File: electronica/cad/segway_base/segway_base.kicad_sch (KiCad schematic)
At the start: 145 parts, among them J1 XT60PW-M 1=P− 2=P+, J10 XH-6 mot+enc DER, J11 Motor IZQ a módulo, J12 Motor DER a módulo, J13 Servo IZQ JR, J14 Servo DER JR, J15 UBEC entrada, J16 UBEC salida bornera, J17 UBEC salida enchufe, J18 Voltímetro ROB-004, J19 LM2596 entrada, J2 MKDS3 batería alt., J20 LM2596 salida 5V, J21 Shunt INA219 IZQ 1=Vin− 2=Vin+, J22 Shunt INA219 DER 1=Vin− 2=Vin+, J3 Lazo interruptor+paro, J4 Paro XH-3, J5 POWER DRV IZQ, J6 POWER DRV DER, J7 Encoder IZQ XH-4, J8 Encoder DER XH-4, J9 XH-6 mot+enc IZQ, Q1 IRF4905

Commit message: electronica: esquema v0.3 con Blue Pill STM32F103C8T6 (ELE-020)
- Especificación v0.3: 153 componentes, 63 nets, 7 símbolos de módulos;
  módulos enchufados en zócalos de 2,54 mm y motores en borneras (DEC-13).
- Encoders en TIM2/TIM4, PWM de motores en TIM3, servos en TIM1, I2C2,
  rail 3V3 de periféricos con mini buck ROB-005.
- Datasheet STM32F103 DS5319 y material de la Blue Pill archivados.
- ERC 0 errores/0 avisos y netlist igual a la especificación.

Co-Authored-By: Claude Opus 5.5 <noreply@anthropic.com>
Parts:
- removed A1: ESP32-DevKitC-32E (prov.), symbol segway_modulos:ROB-012_ESP32-DevKitC-V4_38p
- removed A3: DRV8871 mód. IZQ, Connector_PinSocket_2.54mm:PinSocket_1x04_P2.54mm_Vertical, symbol segway_modulos:ROB-008_DRV8871_modulo_4p
- removed A4: DRV8871 mód. DER (prov.), Connector_PinSocket_2.54mm:PinSocket_1x04_P2.54mm_Vertical, symbol segway_modulos:ROB-008_DRV8871_modulo_4p
- removed A5: INA219 MCU-219 0x41 IZQ, Connector_PinSocket_2.54mm:PinSocket_1x06_P2.54mm_Vertical, symbol segway_modulos:ROB-002_INA219_MCU-219_6p
- removed A6: INA219 MCU-219 0x44 DER, Connector_PinSocket_2.54mm:PinSocket_1x06_P2.54mm_Vertical, symbol segway_modulos:ROB-002_INA219_MCU-219_6p
- removed J1: XT60PW-M 1=P− 2=P+, Connector_AMASS:AMASS_XT60PW-M_1x02_P7.20mm_Horizontal, symbol Connector_Generic:Conn_01x02
- removed J10: XH-6 mot+enc DER, Connector_JST:JST_XH_B6B-XH-A_1x06_P2.50mm_Vertical, symbol Connector_Generic:Conn_01x06
- removed J17: UBEC salida enchufe, Connector_PinHeader_2.54mm:PinHeader_1x03_P2.54mm_Vertical, symbol Connector_Generic:Conn_01x03
- removed J19: LM2596 entrada, TerminalBlock_Phoenix:TerminalBlock_Phoenix_MKDS-1,5-2-5.08_1x02_P5.08mm_Horizontal, symbol Connector:Screw_Terminal_01x02
- removed J2: MKDS3 batería alt., TerminalBlock_Phoenix:TerminalBlock_Phoenix_MKDS-3-2-5.08_1x02_P5.08mm_Horizontal, symbol Connector:Screw_Terminal_01x02
- removed J20: LM2596 salida 5V, TerminalBlock_Phoenix:TerminalBlock_Phoenix_MKDS-1,5-2-5.08_1x02_P5.08mm_Horizontal, symbol Connector:Screw_Terminal_01x02
- removed J4: Paro XH-3, Connector_JST:JST_XH_B3B-XH-A_1x03_P2.50mm_Vertical, symbol Connector_Generic:Conn_01x03
- removed J7: Encoder IZQ XH-4, Connector_JST:JST_XH_B4B-XH-A_1x04_P2.50mm_Vertical, symbol Connector_Generic:Conn_01x04
- removed J8: Encoder DER XH-4, Connector_JST:JST_XH_B4B-XH-A_1x04_P2.50mm_Vertical, symbol Connector_Generic:Conn_01x04
- removed J9: XH-6 mot+enc IZQ, Connector_JST:JST_XH_B6B-XH-A_1x06_P2.50mm_Vertical, symbol Connector_Generic:Conn_01x06
- removed JP2: AD0 1-2=GND, Jumper:SolderJumper-3_P1.3mm_Bridged12_RoundedPad1.0x1.5mm, symbol Jumper:SolderJumper_3_Bridged12
- added A1: Blue Pill STM32F103C8T6, symbol segway_modulos:ROB-012_BluePill_STM32F103C8_40p
- added A10: LM2596 ROB-001 5V (respaldo), symbol segway_modulos:ROB-001_LM2596_modulo_4p
- added A3: DRV8871 mód. IZQ (enchufable), symbol segway_modulos:ROB-008_DRV8871_modulo_8p
- added A4: DRV8871 mód. DER (prov., enchufable), symbol segway_modulos:ROB-008_DRV8871_modulo_8p
- added A5: INA219 MCU-219 0x41 IZQ, symbol segway_modulos:ROB-002_INA219_MCU-219_8p
- added A6: INA219 MCU-219 0x44 DER, symbol segway_modulos:ROB-002_INA219_MCU-219_8p
- added A9: Mini buck 3,3V ROB-005 (3V3_PER), symbol segway_modulos:ROB-005-006_MiniBuck_modulo_4p
- added C27: 10µ/10V X7R, Capacitor_SMD:C_1206_3216Metric_Pad1.33x1.80mm_HandSolder, symbol Device:C
- added C28: 100n/50V X7R, Capacitor_SMD:C_0805_2012Metric_Pad1.18x1.45mm_HandSolder, symbol Device:C
- added J1: Batería MKDS3 1=P− 2=P+, TerminalBlock_Phoenix:TerminalBlock_Phoenix_MKDS-3-2-5.08_1x02_P5.08mm_Horizontal, symbol Connector:Screw_Terminal_01x02
- added J23: UART1 1=GND 2=TX 3=RX, Connector_PinHeader_2.54mm:PinHeader_1x03_P2.54mm_Vertical, symbol Connector_Generic:Conn_01x03
- added J4: Paro MPT0,5 1=GND 2=NC 3=AUX, TerminalBlock_Phoenix:TerminalBlock_Phoenix_MPT-0,5-3-2.54_1x03_P2.54mm_Horizontal, symbol Connector:Screw_Terminal_01x03
- added J7: Encoder IZQ PT1,5 1=GND 2=A 3=B 4=V, TerminalBlock_Phoenix:TerminalBlock_Phoenix_PT-1,5-4-3.5-H_1x04_P3.50mm_Horizontal, symbol Connector:Screw_Terminal_01x04
- added J8: Encoder DER PT1,5 1=GND 2=A 3=B 4=V, TerminalBlock_Phoenix:TerminalBlock_Phoenix_PT-1,5-4-3.5-H_1x04_P3.50mm_Horizontal, symbol Connector:Screw_Terminal_01x04
- added R32: 0 (3V3_MCU↔3V3_PER), Resistor_SMD:R_0805_2012Metric_Pad1.20x1.40mm_HandSolder, symbol Device:R
- added R33, R34: 1k, Resistor_SMD:R_0805_2012Metric_Pad1.20x1.40mm_HandSolder, symbol Device:R
- added R35, R36, R37, R38: 4k7 1%, Resistor_SMD:R_0805_2012Metric_Pad1.20x1.40mm_HandSolder, symbol Device:R
- added R39: 0 (AD0→GND), Resistor_SMD:R_0805_2012Metric_Pad1.20x1.40mm_HandSolder, symbol Device:R
- added R40: 1k (AD0→3V3_PER), Resistor_SMD:R_0805_2012Metric_Pad1.20x1.40mm_HandSolder, symbol Device:R
- added TP41: TP_3V3_MCU, TestPoint:TestPoint_Loop_D2.50mm_Drill1.0mm, symbol Connector:TestPoint
- A2: Estado provisorio [H] (orden de pines [V]/[M]; zócalo estándar 1x08; contorno del módulo pendiente de medida) -> provisorio [H] (orden de pines [V]/[M]; zócalo estándar 1x08 (DEC-13); alimentado desde 3V3_PER; contorno del módulo pendiente de medida; codificación propuesta: retirar el pin 5 (XDA, sin uso) de la tira macho y tapar la posición 5 del zócalo, porque invertido llevaría 3V3_PER a INT y el VCC del módulo a PB14)
- A7: Estado provisorio [H] (orden [V]; dirección de fábrica 0x40 [H], sujeta a aprobar el cambio del contrato §4.1; ubicación en la rama lógica = propuesta [H] que se desvía de [ENERGIA] §5.2 (INA226 en el bus), pendiente de Matías, REQ-14; unión VBS-IN− interna pendiente E-01) -> provisorio [H] (orden [V]; dirección de fábrica 0x40 [H], sujeta a aprobar el cambio del contrato §4.1; ubicación en la rama lógica = propuesta [H] que se desvía de [ENERGIA] §5.2 (INA226 en el bus), pendiente de Matías, REQ-14; unión VBS-IN− interna pendiente E-01; la 1x08 no tiene pin libre para codificar: invertido lleva VM_LOG_F a VCC (6 V abs.) y deja el shunt entre 3V3_PER y GND, así que la huella lleva un tope mecánico contra el cuerpo invertido y el contorno serigrafiado); Fuente [CAP]/ROB-009_INA226/referencia_compra.png [V]; [DS-226] p.3, p.5, p.15, p.18 Tabla 6-2, p.26-28; [ENERGIA] §5.1 (R100 solo apto para lógica) -> [CAP]/ROB-009_INA226/referencia_compra.png [V]; [DS-226] p.3, p.5, p.15, p.18 Tabla 6-2, p.26-28; [ENERGIA] §5.1 (R100 solo apto para lógica); [DS-226] p.4 §5.1 (VS 6 V abs.)
- A8: Estado pendiente de medida (propuesta de [ENERGIA] §10.1, pendiente de Matías; chip no identificado; huella sin medir; validar en E-02) -> pendiente de medida (propuesta de [ENERGIA] §10.1, pendiente de Matías; chip no identificado; huella de 4 PinSocket_1x01 en las esquinas medidas, a crear tras E-01 (DEC-13); validar en E-02; cuatro esquinas: girado 180° une VM_LOG con 5V por la masa del módulo e invierte su entrada, así que la huella necesita codificación mecánica (propuesta 16); zócalos superpuestos con los de A10 para que no entren los dos)
- C10, C11, C12, C13: Estado provisorio [H] (DNP; el pad recibe 2 kΩ como resistencia in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 -> provisorio [H] (DNP; 2 kΩ en el pad solo si E-04 confirma s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; Fuente [DS-ESP32] p.38-39 (filtro del PCNT) -> [RM0008] §13.3 (filtro digital ICxF del timer); divisor 1k/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
- C14: Fuente [DS-ESP32] p.43 Tabla 4-3 (100 nF de ensayo) -> [DS-STM32] p.75 Ecuación 1 (carga del capacitor de muestreo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
- C15: Fuente Filtro RC [H]: activación (contacto abierto) τ = (R24 + R25)·C15 ≈ 1,1 ms, ≈1,5 ms hasta VIH = 0,75·VDD; liberación τ = R25·C15 = 0,1 ms -> Filtro RC [H]: activación (contacto abierto) τ = (R24 + R25)·C15 ≈ 1,1 ms, ≈1,15 ms hasta VIH = 2,145 V; liberación τ = R25·C15 = 0,1 ms
- C25: Fuente [DS-ESP32] p.19, p.52 -> [STM32-BASE] (pin 5V = VBUS sin protección); [SCH-BP] (C5 1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
- C26: Estado provisorio [H] (DNP) -> provisorio [H] (DNP; ahora en 3V3_MCU); Fuente LDO AMS1117 de la placa: estabilidad con cerámicos no docum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 -> [SCH-BP] (C6 10 µF + C8 100 nF ya en la salida del LDO de l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
- D2: Estado provisorio [H] (no reemplazar por 0 Ω salvo verificar que e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 -> provisorio [H] (obligatoria, nunca 0 Ω: impide que el USB a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; Fuente [SCH-DevKitC] (D3 BAT760-7 VBUS→EXT_5V); [CONTRATO] §2.11(b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 -> [SCH-BP] (VBUS del micro-USB unido directo al pin 5V); [STM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
- D3: DNP si -> (none); Estado provisorio [H] (DNP con Q1) -> provisorio [H] (montado con Q1; limita VGS a 12 V); now fitted
- F2: value ATM lento PEND (antec. 5A) -> ATM lento PEND (≤4 A); Estado provisorio [H] (valor tras E-04 y ≤ corriente admisible de 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 -> provisorio [H] (≤ 4 A por los zócalos de A3 y A5: 2 contact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
- F3: value ATM lento PEND (antec. 5A) -> ATM lento PEND (≤4 A); Estado provisorio [H] (valor tras E-04 y ≤ corriente admisible de 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 -> provisorio [H] (≤ 4 A por los zócalos de A4 y A6; valor tra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
- F5: value ATM lento PEND -> ATM rápido PEND (prop. ≤1A); Estado provisorio [H] (valor tras E-02; decisión 8 de [ENERGIA] §1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 -> provisorio [H] (propuesta 17: ≤ 1 A de acción rápida, que a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; Fuente [ENERGIA] §2.2 (fila Lógica) -> [ENERGIA] §2.2 (fila Lógica); consumo de la rama ≈0,1 A [H]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
- J11: value Motor IZQ a módulo -> Motor IZQ 1=M− 2=M+; DNP si -> (none); Estado provisorio [H] (DNP; solo con J9/J10, cuyo orden es [H]) -> provisorio [H] (montada; 1 = M− blanco = OUT2, 2 = M+ rojo 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; Fuente [DS-DRV] p.3 (OUT1/OUT2); [INV] ROB-011 (rojo M+, blanco M−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 -> DEC-13 [M] (borneras para motores); DEC-01 [M] (rojo M+, bl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; now fitted
- J12: value Motor DER a módulo -> Motor DER 1=M− 2=M+; DNP si -> (none); Estado provisorio [H] (DNP; solo con J9/J10, cuyo orden es [H]) -> provisorio [H] (montada; 1 = M− blanco = OUT2, 2 = M+ rojo 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; Fuente [DS-DRV] p.3 (OUT1/OUT2); [INV] ROB-011 (rojo M+, blanco M−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 -> Igual que J11; now fitted
- J13, J14: Estado provisorio [H] (orden JR GND-V+-SIG [D distribuidor], verificar en el ejemplar E-01/E-05; contacto de 2,54 mm ≈3 A [H] < bloqueo 3,1-3,9 A: medir la temperatura del contacto con el servo bloqueado en E-05/E-06) -> provisorio [H] (orden JR GND-V+-SIG [D distribuidor], verificar en el ejemplar E-01/E-05; contacto de 2,54 mm ≈3 A [H] < bloqueo 3,1-3,9 A: medir la temperatura del contacto con el servo bloqueado en E-05/E-06; serigrafiar 'S + −' y los colores del cable junto al header)
- J15: Estado provisorio [H] (tipo de enchufe pendiente) -> provisorio [H] (montada; se corta el enchufe rojo de 2 pine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; Fuente [CAP]/ROB-007_YSIDO_UBEC_6A/referencia_compra.png [V] -> [CAP]/ROB-007_YSIDO_UBEC_6A/referencia_compra.png [V]; DEC-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
- J16: value UBEC salida bornera -> UBEC salida 6V PT1,5 1=GND 2=V+; footprint TerminalBlock_Phoenix:TerminalBlock_Phoenix_MKDS-1,5-2-5.08_1x02_P5.08mm_Horizontal -> TerminalBlock_Phoenix:TerminalBlock_Phoenix_PT-1,5-2-3.5-H_1x02_P3.50mm_Horizontal; DNP si -> (none); Estado provisorio [H] (DNP; necesaria para operar con dos servos p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 -> provisorio [H] (montada; se corta el JR de salida del UBEC;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; Fuente [DS-SERVO] p.3 tabla 3-4 (bloqueo 3,1-3,9 A) -> DEC-13 [M]; [DS-SERVO] p.3 tabla 3-4 (bloqueo 3,9 A por ser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; now fitted
- J21: DNP (none) -> si; Estado provisorio [H] (cable a la bornera del módulo A5; corriente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 -> provisorio [H] (DNP; respaldo si el módulo A5 conserva su b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; now not fitted
- J22: DNP (none) -> si; Estado provisorio [H] (cable a la bornera del módulo A6; corriente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 -> provisorio [H] (DNP; respaldo si el módulo A6 conserva su b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; now not fitted
- J3: Estado provisorio [H] (REQ-17 abierto) -> provisorio [H] (REQ-17 abierto; igual tipo que J1: separarl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
- J5: value POWER DRV IZQ -> POWER DRV IZQ (opción A); DNP (none) -> si; Estado provisorio [H] -> provisorio [H] (DNP; solo en la opción A: módulo con sus bo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; now not fitted
- J6: value POWER DRV DER -> POWER DRV DER (opción A); DNP (none) -> si; Estado provisorio [H] -> provisorio [H] (DNP; solo en la opción A); now not fitted
- JP1: DNP (none) -> si; Estado provisorio [H] (excluyente con Q1; con JP1 la única protecc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 -> provisorio [H] (DNP; solo si Matías elige un XT60 en latigu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; now not fitted
- JP3: value SDA INA 1-2=I2C0 -> SDA INA 1-2=I2C2; Estado provisorio [H] (decisión tras E-08) -> provisorio [H] (1-2 = INA en I2C2, opción A; 2-3 = I2C1 rem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
- JP4: value SCL INA 1-2=I2C0 -> SCL INA 1-2=I2C2; Estado provisorio [H] (decisión tras E-08) -> provisorio [H] (1-2 = INA en I2C2, opción A; 2-3 = I2C1 rem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
- Q1: DNP si -> (none); Estado provisorio [H] (DNP; decisiones 3 y 9 de [ENERGIA] §10; a 1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 -> provisorio [H] (montado por defecto: con J1 en bornera es l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; now fitted
- R1: Estado provisorio [H] (decisión 14 de [ENERGIA] §10 pendiente de M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 -> provisorio [H] (lado MCU de R35; 2,2 kΩ cubre un pull-up in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; Fuente [ENERGIA] §8.1; [CONTRATO] §5.3; [DS-ESP32] p.52; [DS-DRV] 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 -> [DS-STM32] p.61 Tabla 36 (RPU 30-50 kΩ, fuga ±1 µA); [RM000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
- R10, R11, R12, R9: Fuente [CONTRATO] §2.4; [ENERGIA] §6.5; [DS-ESP32] p.52-53 -> [CONTRATO] §2.4; [ENERGIA] §6.5; [DS-STM32] Tabla 7 p.37 (i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
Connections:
- net 5V: now also A10.3 (OUT+)
- net CICLO_SCL1: now also A1.16 (PB8)
- net ENC_DER_A: now also J8.2 (Pin_2)
- net ENC_DER_A_MCU: now also A1.14 (PB6)
- net ENC_DER_B: now also J8.3 (Pin_3)
- net ENC_DER_B_MCU: now also A1.15 (PB7)
- net ENC_IZQ_A: now also J7.2 (Pin_2)
- net ENC_IZQ_A_MCU: now also A1.25 (PA0)
- net ENC_IZQ_B: now also J7.3 (Pin_3)
- net ENC_IZQ_B_MCU: now also A1.26 (PA1)
- net GND: now also A1.19 (GND), A1.39 (GND), A10.2 (IN-), A10.4 (OUT-), A3.1 (GND), A3.6 (POWER-), A4.1 (GND), A4.6 (POWER-), A5.2 (Gnd), A6.2 (Gnd), A9.2 (IN-), A9.4 (OUT-)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
- net I2C_SCL: now also A1.35 (PB10)
- net I2C_SDA: now also A1.36 (PB11)
- net IMU_AD0: now also R39.2, R40.2
- net IMU_INT: now also A1.3 (PB14)
- net IN1_DER: now also A4.3 (IN1), R37.2; no longer R3.1
- net IN1_IZQ: now also A3.3 (IN1), R35.2; no longer R1.1
- net IN2_DER: now also A4.4 (IN2), R38.2; no longer R4.1
- net IN2_IZQ: now also A3.4 (IN2), R36.2; no longer R2.1
- net INA_ALERT: now also A1.2 (PB13)
- net INA_SCL: now also A5.3 (Scl), A6.3 (Scl)
- net INA_SDA: now also A5.4 (Sda), A6.4 (Sda)
- net LED_ESTADO: now also A1.13 (PB5)
- net MOT_DER_1: now also J12.2 (Pin_2), A4.7 (OUT1); no longer J12.1 (Pin_1)
- net MOT_DER_2: now also J12.1 (Pin_1), A4.8 (OUT2); no longer J12.2 (Pin_2)
- net MOT_IZQ_1: now also J11.2 (Pin_2), A3.7 (OUT1); no longer J11.1 (Pin_1)
- net MOT_IZQ_2: now also J11.1 (Pin_1), A3.8 (OUT2); no longer J11.2 (Pin_2)
- net PARO_AUX: now also J4.3 (Pin_3)
- net PARO_CONT: now also J4.2 (Pin_2)
- net PARO_MCU: now also A1.1 (PB12)
- net RESERVA_SDA1: now also A1.17 (PB9)
- net SERVO_DER_MCU: now also A1.4 (PB15)
- net SERVO_IZQ_MCU: now also A1.5 (PA8)
- net VBAT_ADC: now also A1.28 (PA3)
- net VBAT_P: now also J1.2 (Pin_2)
- net VM_DER: now also A4.2 (VM), A4.5 (POWER+), A6.5 (Vin-), A6.7 (Vin-_born)
- net VM_DER_F: now also A6.6 (Vin+), A6.8 (Vin+_born)
- net VM_IZQ: now also A3.2 (VM), A3.5 (POWER+), A5.5 (Vin-), A5.7 (Vin-_born)
- net VM_IZQ_F: now also A5.6 (Vin+), A5.8 (Vin+_born)
- net VM_LOG: now also A10.1 (IN+), A9.1 (IN+), C28.1
- net V_ENC: now also J7.4 (Pin_4), J8.4 (Pin_4)
- net 3V3 renamed 3V3_PER
- net 3V3_PER: now also A5.1 (Vcc), A6.1 (Vcc), A9.3 (OUT+), C27.1, R32.2, R40.1; no longer C26.1, R24.1
- net 5V_ESP renamed 5V_MCU
- net 5V_MCU: now also A1.18 (5V)
- new net 3V3_MCU: A1.20 (3V3), A1.21 (VBAT), A1.38 (3V3), C26.1, R24.1, R32.1, TP41.1
- new net IN1_DER_MCU: A1.33 (PB0), R3.1, R37.1
- new net IN1_IZQ_MCU: A1.31 (PA6), R1.1, R35.1
- new net IN2_DER_MCU: A1.34 (PB1), R38.1, R4.1
- new net IN2_IZQ_MCU: A1.32 (PA7), R2.1, R36.1
- new net UART1_RX: J23.3 (Pin_3), R34.1
- new net UART1_RX_MCU: A1.7 (PA10), R34.2
- new net UART1_TX: J23.2 (Pin_2), R33.2
- new net UART1_TX_MCU: A1.6 (PA9), R33.1
- no-connect marks 23 -> 15
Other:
- note added: "BLUE PILL STM32"
- note removed: "CONTROLADOR ESP32 (PROVISORIO)"

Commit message: electronica: esquema v0.4 simplificado y PCB v0.1 en curso (pausa)
- Especificación v0.4: 60 componentes y 47 nets para placa casera
  (sin puntos de prueba ni alternativas no montadas); ERC 0 y netlist igual.
- Huellas de los 7 módulos en segway_modulos.pretty.
- Reglas de fabricación casera, 71 supuestos (supuestos.md / .json).
- Constructor de PCB construir_pcb.py y flujo guardado; placa a medio
  rutear. Instrucciones de reanudación en estado_actual.md (ELE-032).

Co-Authored-By: Claude Opus 5.5 <noreply@anthropic.com>
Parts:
- removed A10: LM2596 ROB-001 5V (respaldo), symbol segway_modulos:ROB-001_LM2596_modulo_4p
- removed C10, C11, C12, C13: 1n/50V C0G, Capacitor_SMD:C_0805_2012Metric_Pad1.18x1.45mm_HandSolder, symbol Device:C
- removed C15, C16, C17, C18, C19, C20, C21, C22, C23, C28, C6, C7: 100n/50V X7R, Capacitor_SMD:C_0805_2012Metric_Pad1.18x1.45mm_HandSolder, symbol Device:C
- removed C2: 470µ/35V low-ESR, Capacitor_THT:CP_Radial_D10.0mm_P5.00mm, symbol Device:C_Polarized
- removed C24: 47µ/35V, Capacitor_THT:CP_Radial_D6.3mm_P2.50mm, symbol Device:C_Polarized
- removed C25: 10µ/25V X7R, Capacitor_SMD:C_1206_3216Metric_Pad1.33x1.80mm_HandSolder, symbol Device:C
- removed C26, C27: 10µ/10V X7R, Capacitor_SMD:C_1206_3216Metric_Pad1.33x1.80mm_HandSolder, symbol Device:C
- removed D1: SMAJ15A, Diode_SMD:D_SMA, symbol Diode:SMAJ15A
- removed D2: SS34 (SMA 3A/40V), Diode_SMD:D_SMA, symbol Diode:SS34
- removed D5: LED verde GaP 3mm Vf≈2,1V, LED_THT:LED_D3.0mm, symbol Device:LED
- removed J21: Shunt INA219 IZQ 1=Vin− 2=Vin+, TerminalBlock_Phoenix:TerminalBlock_Phoenix_MKDS-1,5-2-5.08_1x02_P5.08mm_Horizontal, symbol Connector:Screw_Terminal_01x02
- removed J22: Shunt INA219 DER 1=Vin− 2=Vin+, TerminalBlock_Phoenix:TerminalBlock_Phoenix_MKDS-1,5-2-5.08_1x02_P5.08mm_Horizontal, symbol Connector:Screw_Terminal_01x02
- removed J4: Paro MPT0,5 1=GND 2=NC 3=AUX, TerminalBlock_Phoenix:TerminalBlock_Phoenix_MPT-0,5-3-2.54_1x03_P2.54mm_Horizontal, symbol Connector:Screw_Terminal_01x03
- removed J5: POWER DRV IZQ (opción A), TerminalBlock_Phoenix:TerminalBlock_Phoenix_MKDS-1,5-2-5.08_1x02_P5.08mm_Horizontal, symbol Connector:Screw_Terminal_01x02
- removed J6: POWER DRV DER (opción A), TerminalBlock_Phoenix:TerminalBlock_Phoenix_MKDS-1,5-2-5.08_1x02_P5.08mm_Horizontal, symbol Connector:Screw_Terminal_01x02
- removed JP1: Puente 2,5 mm², Connector_Wire:SolderWire-2.5sqmm_1x02_P7.2mm_D2.4mm_OD3.6mm, symbol Jumper:Jumper_2_Bridged
- removed JP3: SDA INA 1-2=I2C2, Jumper:SolderJumper-3_P1.3mm_Bridged12_RoundedPad1.0x1.5mm, symbol Jumper:SolderJumper_3_Bridged12
- removed JP4: SCL INA 1-2=I2C2, Jumper:SolderJumper-3_P1.3mm_Bridged12_RoundedPad1.0x1.5mm, symbol Jumper:SolderJumper_3_Bridged12
- removed JP6: Bypass shunt IZQ, Connector_Wire:SolderWire-0.5sqmm_1x02_P4.6mm_D0.9mm_OD2.1mm, symbol Jumper:Jumper_2_Open
- removed JP7: Bypass shunt DER, Connector_Wire:SolderWire-0.5sqmm_1x02_P4.6mm_D0.9mm_OD2.1mm, symbol Jumper:Jumper_2_Open
- removed JP8: Bypass INA226 (abierto), Jumper:SolderJumper-2_P1.3mm_Open_RoundedPad1.0x1.5mm, symbol Jumper:SolderJumper_2_Open
- removed R10, R11, R12, R9: 1k 1%, Resistor_SMD:R_0805_2012Metric_Pad1.20x1.40mm_HandSolder, symbol Device:R
- removed R17, R18, R19, R20: 3k3, Resistor_SMD:R_0805_2012Metric_Pad1.20x1.40mm_HandSolder, symbol Device:R
- removed R21: 10k, Resistor_SMD:R_0805_2012Metric_Pad1.20x1.40mm_HandSolder, symbol Device:R
- removed R25, R33, R34: 1k, Resistor_SMD:R_0805_2012Metric_Pad1.20x1.40mm_HandSolder, symbol Device:R
- removed R26: 100, Resistor_SMD:R_0805_2012Metric_Pad1.20x1.40mm_HandSolder, symbol Device:R
- removed R27: 470, Resistor_SMD:R_0805_2012Metric_Pad1.20x1.40mm_HandSolder, symbol Device:R
- removed R30: 0 (3V3_PER→V_ENC), Resistor_SMD:R_0805_2012Metric_Pad1.20x1.40mm_HandSolder, symbol Device:R
- removed R31: 0 (5V→V_ENC), Resistor_SMD:R_0805_2012Metric_Pad1.20x1.40mm_HandSolder, symbol Device:R
- removed R32: 0 (3V3_MCU↔3V3_PER), Resistor_SMD:R_0805_2012Metric_Pad1.20x1.40mm_HandSolder, symbol Device:R
- removed R39: 0 (AD0→GND), Resistor_SMD:R_0805_2012Metric_Pad1.20x1.40mm_HandSolder, symbol Device:R
- removed R40: 1k (AD0→3V3_PER), Resistor_SMD:R_0805_2012Metric_Pad1.20x1.40mm_HandSolder, symbol Device:R
- removed TP1: TP_VBAT, TestPoint:TestPoint_Loop_D2.50mm_Drill1.0mm, symbol Connector:TestPoint
- removed TP10: TP_3V3_PER, TestPoint:TestPoint_Loop_D2.50mm_Drill1.0mm, symbol Connector:TestPoint
- removed TP11: TP_GND_PWR, TestPoint:TestPoint_Loop_D2.50mm_Drill1.0mm, symbol Connector:TestPoint
- removed TP12: TP_GND_LOG, TestPoint:TestPoint_Loop_D2.50mm_Drill1.0mm, symbol Connector:TestPoint
- removed TP13: TP_GND_SERVO, TestPoint:TestPoint_Loop_D2.50mm_Drill1.0mm, symbol Connector:TestPoint
- removed TP14: TP_VM_UBEC, TestPoint:TestPoint_Loop_D2.50mm_Drill1.0mm, symbol Connector:TestPoint
- removed TP15: TP_SHUNT+_IZQ, TestPoint:TestPoint_THTPad_D2.0mm_Drill1.0mm, symbol Connector:TestPoint
- removed TP16: TP_SHUNT+_DER, TestPoint:TestPoint_THTPad_D2.0mm_Drill1.0mm, symbol Connector:TestPoint
- removed TP17: TP_SHUNT+_LOG, TestPoint:TestPoint_THTPad_D2.0mm_Drill1.0mm, symbol Connector:TestPoint
- removed TP18: TP_SHUNT-_LOG, TestPoint:TestPoint_THTPad_D2.0mm_Drill1.0mm, symbol Connector:TestPoint
- removed TP19: TP_IN1_IZQ, TestPoint:TestPoint_THTPad_D2.0mm_Drill1.0mm, symbol Connector:TestPoint
- removed TP2: TP_VBAT_SW, TestPoint:TestPoint_Loop_D2.50mm_Drill1.0mm, symbol Connector:TestPoint
- removed TP20: TP_IN2_IZQ, TestPoint:TestPoint_THTPad_D2.0mm_Drill1.0mm, symbol Connector:TestPoint
- removed TP21: TP_IN1_DER, TestPoint:TestPoint_THTPad_D2.0mm_Drill1.0mm, symbol Connector:TestPoint
- removed TP22: TP_IN2_DER, TestPoint:TestPoint_THTPad_D2.0mm_Drill1.0mm, symbol Connector:TestPoint
- removed TP23: TP_A_IZQ, TestPoint:TestPoint_THTPad_D2.0mm_Drill1.0mm, symbol Connector:TestPoint
- removed TP24: TP_B_IZQ, TestPoint:TestPoint_THTPad_D2.0mm_Drill1.0mm, symbol Connector:TestPoint
- removed TP25: TP_A_DER, TestPoint:TestPoint_THTPad_D2.0mm_Drill1.0mm, symbol Connector:TestPoint
- removed TP26: TP_B_DER, TestPoint:TestPoint_THTPad_D2.0mm_Drill1.0mm, symbol Connector:TestPoint
- removed TP27: TP_S_IZQ, TestPoint:TestPoint_THTPad_D2.0mm_Drill1.0mm, symbol Connector:TestPoint
- removed TP28: TP_S_DER, TestPoint:TestPoint_THTPad_D2.0mm_Drill1.0mm, symbol Connector:TestPoint
- removed TP29: TP_SDA, TestPoint:TestPoint_THTPad_D2.0mm_Drill1.0mm, symbol Connector:TestPoint
- removed TP3: TP_VM_IZQ, TestPoint:TestPoint_Loop_D2.50mm_Drill1.0mm, symbol Connector:TestPoint
- removed TP30: TP_SCL, TestPoint:TestPoint_THTPad_D2.0mm_Drill1.0mm, symbol Connector:TestPoint
- removed TP31: TP_SDA_INA, TestPoint:TestPoint_THTPad_D2.0mm_Drill1.0mm, symbol Connector:TestPoint
- removed TP32: TP_SCL_INA, TestPoint:TestPoint_THTPad_D2.0mm_Drill1.0mm, symbol Connector:TestPoint
- removed TP33: TP_INT, TestPoint:TestPoint_THTPad_D2.0mm_Drill1.0mm, symbol Connector:TestPoint
- removed TP34: TP_CICLO, TestPoint:TestPoint_THTPad_D2.0mm_Drill1.0mm, symbol Connector:TestPoint
- removed TP35: TP_ALERT, TestPoint:TestPoint_THTPad_D2.0mm_Drill1.0mm, symbol Connector:TestPoint
- removed TP36: TP_VBAT_ADC, TestPoint:TestPoint_THTPad_D2.0mm_Drill1.0mm, symbol Connector:TestPoint
- removed TP37: TP_PARO, TestPoint:TestPoint_THTPad_D2.0mm_Drill1.0mm, symbol Connector:TestPoint
- removed TP38: TP_V_ENC, TestPoint:TestPoint_THTPad_D2.0mm_Drill1.0mm, symbol Connector:TestPoint
- removed TP39: TP_VBAT_P, TestPoint:TestPoint_Loop_D2.50mm_Drill1.0mm, symbol Connector:TestPoint
- removed TP4: TP_VM_DER, TestPoint:TestPoint_Loop_D2.50mm_Drill1.0mm, symbol Connector:TestPoint
- removed TP40: TP_VBAT_F, TestPoint:TestPoint_Loop_D2.50mm_Drill1.0mm, symbol Connector:TestPoint
- removed TP41: TP_3V3_MCU, TestPoint:TestPoint_Loop_D2.50mm_Drill1.0mm, symbol Connector:TestPoint
- removed TP5: TP_UBEC, TestPoint:TestPoint_Loop_D2.50mm_Drill1.0mm, symbol Connector:TestPoint
- removed TP6: TP_VSERVO_IZQ, TestPoint:TestPoint_Loop_D2.50mm_Drill1.0mm, symbol Connector:TestPoint
- removed TP7: TP_VSERVO_DER, TestPoint:TestPoint_Loop_D2.50mm_Drill1.0mm, symbol Connector:TestPoint
- removed TP8: TP_5V, TestPoint:TestPoint_Loop_D2.50mm_Drill1.0mm, symbol Connector:TestPoint
- removed TP9: TP_5V_MCU, TestPoint:TestPoint_Loop_D2.50mm_Drill1.0mm, symbol Connector:TestPoint
- added D1: SA15A (alt. P6KE18A), Diode_THT:D_DO-15_P10.16mm_Horizontal, symbol Diode:1.5KExxA
- added D2: 1N5819, Diode_THT:D_DO-41_SOD81_P10.16mm_Horizontal, symbol Diode:1N5819
- added J4: Paro MPT0,5 1=GND 2=PARO (NC), TerminalBlock_Phoenix:TerminalBlock_Phoenix_MPT-0,5-2-2.54_1x02_P2.54mm_Horizontal, symbol Connector:Screw_Terminal_01x02
- A1: footprint (none) -> segway_modulos:ROB-012_BluePill_STM32F103C8_40p; Estado provisorio [H] (pinout de las 40 posiciones [D]; numeración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 -> provisorio [H]: huella segway_modulos:ROB-012_BluePill_STM3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
- A2: footprint Connector_PinSocket_2.54mm:PinSocket_1x08_P2.54mm_Vertical -> segway_modulos:ROB-013_MPU6050_modulo_8p; Estado provisorio [H] (orden de pines [V]/[M]; zócalo estándar 1x08 (DEC-13); alimentado desde 3V3_PER; contorno del módulo pendiente de medida; codificación propuesta: retirar el pin 5 (XDA, sin uso) de la tira macho y tapar la posición 5 del zócalo, porque invertido llevaría 3V3_PER a INT y el VCC del módulo a PB14) -> provisorio [H] (orden de pines [V]/[M]; zócalo estándar 1x08 (DEC-13); alimentado desde 3V3_PER; contorno del módulo pendiente de medida; codificación propuesta: retirar el pin 5 (XDA, sin uso) de la tira macho y tapar la posición 5 del zócalo, porque invertido llevaría 3V3_PER a INT y el VCC del módulo a PB14) | v0.4: huella segway_modulos:ROB-013_MPU6050_modulo_8p (1x08 + 2 NPTH de 3,2 mm, contorno supuesto); AD0 (pin 7) sin conexión: la pull-down del GY-521 fija 0x68 (SUP-36, SUP-66); sin pistas debajo
- A3: footprint (none) -> segway_modulos:ROB-008_DRV8871_modulo_8p; Estado provisorio [H] (opción B enchufable, a ratificar por Matías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 -> provisorio [H]: opción B fija, con las borneras POWER y MOT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
- A4: footprint (none) -> segway_modulos:ROB-008_DRV8871_modulo_8p; Estado provisorio [H] (módulo no comprado, REQ-06; decisión 10 de [ENERGIA] §10 pendiente; mismas condiciones de la opción B que A3) -> provisorio [H] (módulo no comprado, REQ-06; decisión 10 de [ENERGIA] §10 pendiente; mismas condiciones de la opción B que A3) | v0.4: huella segway_modulos:ROB-008_DRV8871_modulo_8p; segundo módulo por comprar (SUP-33); J6 eliminada (SUP-63)
- A5: footprint (none) -> segway_modulos:ROB-002_INA219_MCU-219_8p; Estado provisorio [H] (orden [V]; dirección 0x41 por puente A0 [H]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 -> provisorio [H]: dirección 0x41 por puente A0 [H], sujeta al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
- A6: footprint (none) -> segway_modulos:ROB-002_INA219_MCU-219_8p; Estado provisorio [H] (dirección 0x44 sujeta al cambio del contrat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 -> provisorio [H]: dirección 0x44 por puente A1 [H], sujeta al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
- A7: footprint Connector_PinSocket_2.54mm:PinSocket_1x08_P2.54mm_Vertical -> segway_modulos:ROB-009_INA226_modulo_8p; Estado provisorio [H] (orden [V]; dirección de fábrica 0x40 [H], sujeta a aprobar el cambio del contrato §4.1; ubicación en la rama lógica = propuesta [H] que se desvía de [ENERGIA] §5.2 (INA226 en el bus), pendiente de Matías, REQ-14; unión VBS-IN− interna pendiente E-01; la 1x08 no tiene pin libre para codificar: invertido lleva VM_LOG_F a VCC (6 V abs.) y deja el shunt entre 3V3_PER y GND, así que la huella lleva un tope mecánico contra el cuerpo invertido y el contorno serigrafiado) -> provisorio [H] (orden [V]; dirección de fábrica 0x40 [H], sujeta a aprobar el cambio del contrato §4.1; ubicación en la rama lógica = propuesta [H] que se desvía de [ENERGIA] §5.2 (INA226 en el bus), pendiente de Matías, REQ-14; unión VBS-IN− interna pendiente E-01; la 1x08 no tiene pin libre para codificar: invertido lleva VM_LOG_F a VCC (6 V abs.) y deja el shunt entre 3V3_PER y GND, así que la huella lleva un tope mecánico contra el cuerpo invertido y el contorno serigrafiado) | v0.4: huella segway_modulos:ROB-009_INA226_modulo_8p con tope NPTH de 3,2 mm (M3x16) contra la inserción invertida; ALERT con pull-up interna de PB13 (R21 eliminada, SUP-71); JP8 eliminado (SUP-67)
- A8: footprint (none) -> segway_modulos:ROB-005-006_MiniBuck_modulo_4p; Estado pendiente de medida (propuesta de [ENERGIA] §10.1, pendient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 -> pendiente de medida [H]: mini buck de 5 V, chip no identifi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
- A9: footprint (none) -> segway_modulos:ROB-005-006_MiniBuck_modulo_4p; Estado provisorio [H] (nuevo, a ratificar: riel 3V3_PER separado d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 -> provisorio [H]: riel 3V3_PER separado del LDO de la Blue Pi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
- C1: Estado provisorio [H] (valor tras E-04/E-08; decisión 9 de [ENERGIA] §10) -> provisorio [H] (valor tras E-04/E-08; decisión 9 de [ENERGIA] §10) | v0.4: C2 eliminado (SUP-63)
- C14: value 100n/50V X7R -> 100n/50V cerámico de disco (104); footprint Capacitor_SMD:C_0805_2012Metric_Pad1.18x1.45mm_HandSolder -> Capacitor_THT:C_Disc_D5.0mm_W2.5mm_P5.00mm; Estado provisorio [H] -> provisorio [H] | v0.4: THT: disco P5,00 en lugar de 0805; Fuente [DS-STM32] p.75 Ecuación 1 (carga del capacitor de muestreo de 8 pF); τ = 1,07 ms -> [DS-STM32] p.75 Ecuación 1 (carga del capacitor de muestreo de 8 pF); τ = 1,07 ms; huella THT de KiCad 10.0.7 (DEC-14, SUP-16)
- C3: value 10µ/50V X7R -> 10µ/50V X7R multicapa radial; footprint Capacitor_SMD:C_1206_3216Metric_Pad1.33x1.80mm_HandSolder -> Capacitor_THT:C_Disc_D7.5mm_W5.0mm_P5.00mm; Estado provisorio [H] -> provisorio [H] | v0.4: THT: multicapa radial P5,00 en lugar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; Fuente [DS-BMS] p.2 nota 3; [ENERGIA] §7 -> [DS-BMS] p.2 nota 3; [ENERGIA] §7; huella THT de KiCad 10.0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
- C4: Estado provisorio [H] (dato del chip, no del módulo; electrolítico propio del módulo pendiente E-01; valor final tras E-04) -> provisorio [H] (dato del chip, no del módulo; electrolítico propio del módulo pendiente E-01; valor final tras E-04) | v0.4: C6 eliminado: el módulo trae 0,1 µF + 22 µF (SUP-69)
- C5: Estado provisorio [H] (dato del chip, no del módulo; electrolítico propio del módulo pendiente E-01; valor final tras E-04) -> provisorio [H] (dato del chip, no del módulo; electrolítico propio del módulo pendiente E-01; valor final tras E-04) | v0.4: C7 eliminado (SUP-69)
- C8, C9: Estado provisorio [H] (valor tras E-05/E-06) -> provisorio [H] (valor tras E-05/E-06) | v0.4: se conserva s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
- F1: value ATO lento PEND (antec. 15A) -> ATO 15A lento; Estado provisorio [H] (valor tras E-08; ubicación en la placa = de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 -> provisorio [H]: ATO de 15 A lento (SUP-46), a confirmar tra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
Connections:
- net ENC_DER_A_MCU is gone; now on net ENC_DER_A: A1.14 (PB6)
- net ENC_DER_B_MCU is gone; now on net ENC_DER_B: A1.15 (PB7)
- net ENC_IZQ_A_MCU is gone; now on net ENC_IZQ_A: A1.25 (PA0)
- net ENC_IZQ_B_MCU is gone; now on net ENC_IZQ_B: A1.26 (PA1)
- net INA_SCL is gone; now on net I2C_SCL: A5.3 (Scl), A6.3 (Scl), A7.5 (SCL)
- net INA_SDA is gone; now on net I2C_SDA: A5.4 (Sda), A6.4 (Sda), A7.6 (SDA)
- net PARO_MCU is gone; now on net PARO_CONT: A1.1 (PB12)
- net UART1_RX_MCU is gone; now on net UART1_RX: A1.7 (PA10)
- net UART1_TX_MCU is gone; now on net UART1_TX: A1.6 (PA9)
- net V_ENC is gone; now on net 3V3_PER: J7.4 (Pin_4), J8.4 (Pin_4)
- net 5V: now also D2.2 (A)
- net 5V_MCU: now also D2.1 (K)
- net GND: now also D1.2 (A2), J4.1 (Pin_1)
- net MOT_DER_1: now also J12.1 (Pin_1); no longer J12.2 (Pin_2)
- net MOT_DER_2: now also J12.2 (Pin_2); no longer J12.1 (Pin_1)
- net MOT_IZQ_1: now also J11.1 (Pin_1); no longer J11.2 (Pin_2)
- net MOT_IZQ_2: now also J11.2 (Pin_2); no longer J11.1 (Pin_1)
- net PARO_CONT: now also J4.2 (Pin_2)
- net VM_BUS: now also D1.1 (A1)
- net CICLO_SCL1: no longer names the net of A1.16 (PB8)
- net IMU_AD0: no longer names the net of A2.7 (AD0)
- net LED_ESTADO: no longer names the net of A1.13 (PB5)
- net RESERVA_SDA1: no longer names the net of A1.17 (PB9)
- no-connect marks 15 -> 19
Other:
- note removed: "PUNTOS DE PRUEBA"

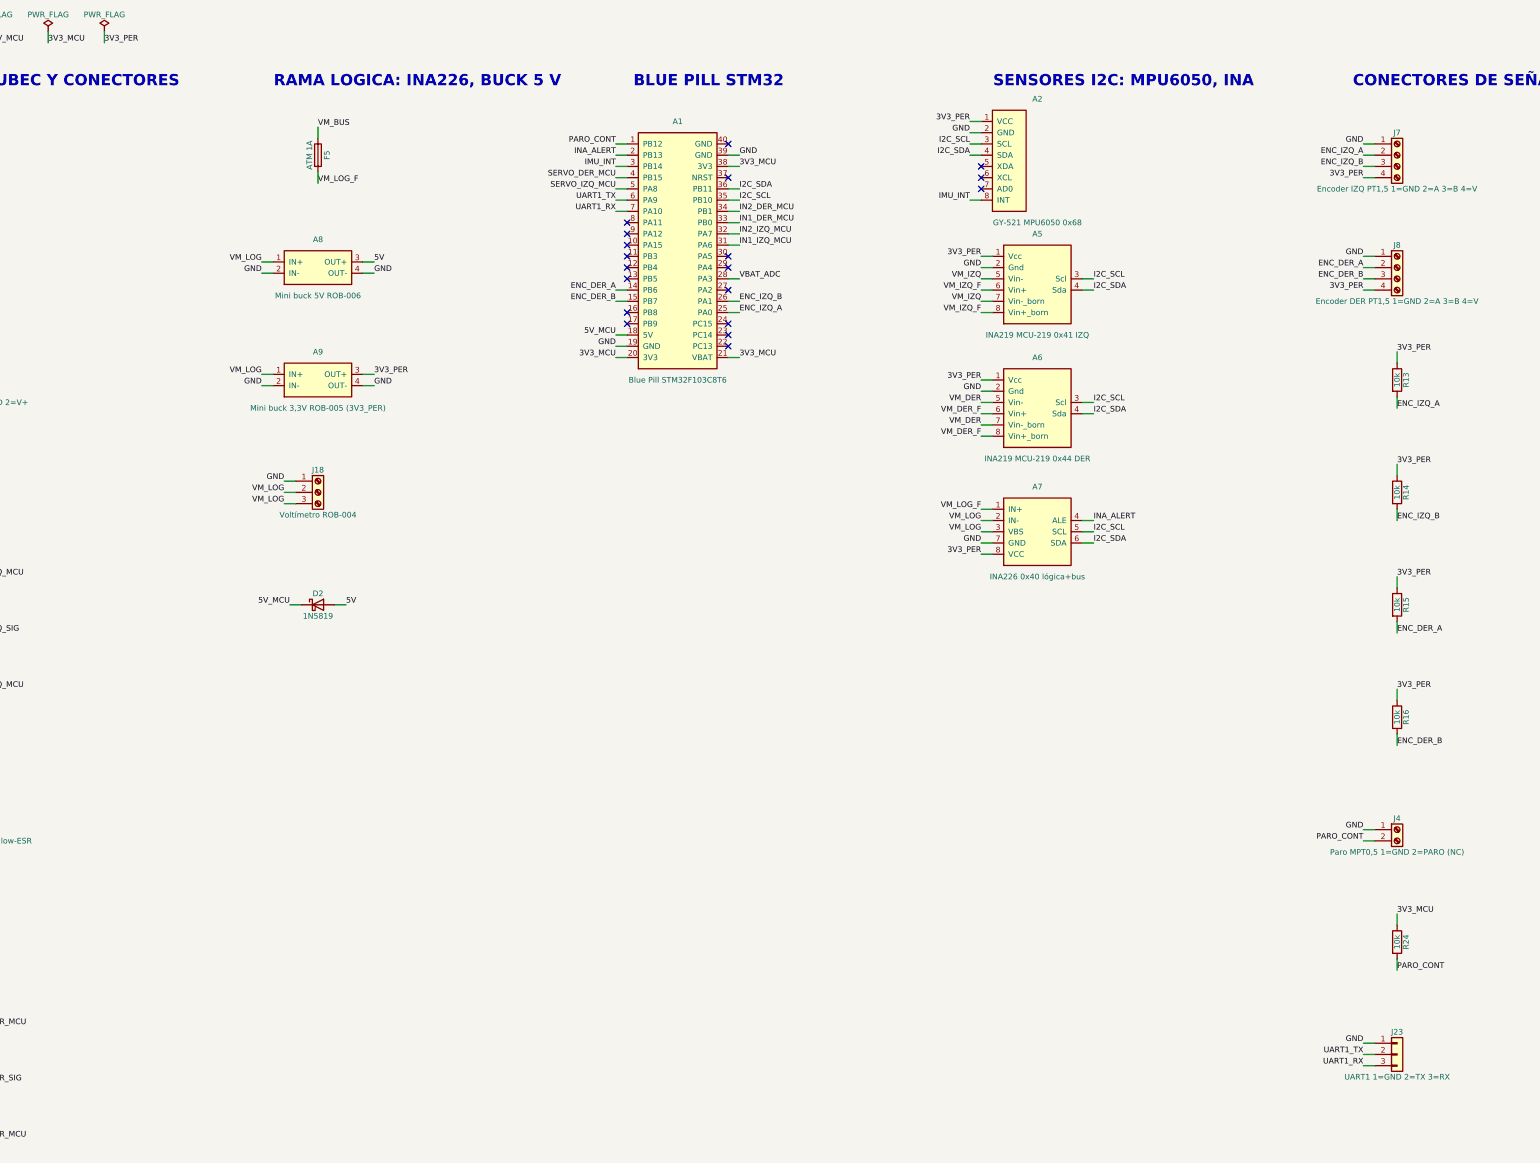
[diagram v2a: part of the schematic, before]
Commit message: electronica: controladora ESP32-S3-DevKitC-1-N16R8 y esquema v0.5 (DEC-16)
- Heemol ESP32-S3-DevKitC-1-N16R8 (ASIN B0FKFXC6F8) reemplaza a la Blue Pill;
  ficha, pinout y medidas del vendedor en ROB-012_ESP32-S3_DevKitC-1_N16R8.
- Símbolo y huella 2x22 a 25,40 mm (SUP-22) con zona sin cobre bajo la antena.
- Especificación v0.5: 58 componentes, sin mini buck de 3,3 V ni header UART;
  esquema regenerado con ERC 0 y netlist igual a la especificación.
- Supuestos SUP-22 a SUP-31, SUP-59 y SUP-70 actualizados.

Co-Authored-By: Claude Opus 5.5 <noreply@anthropic.com>
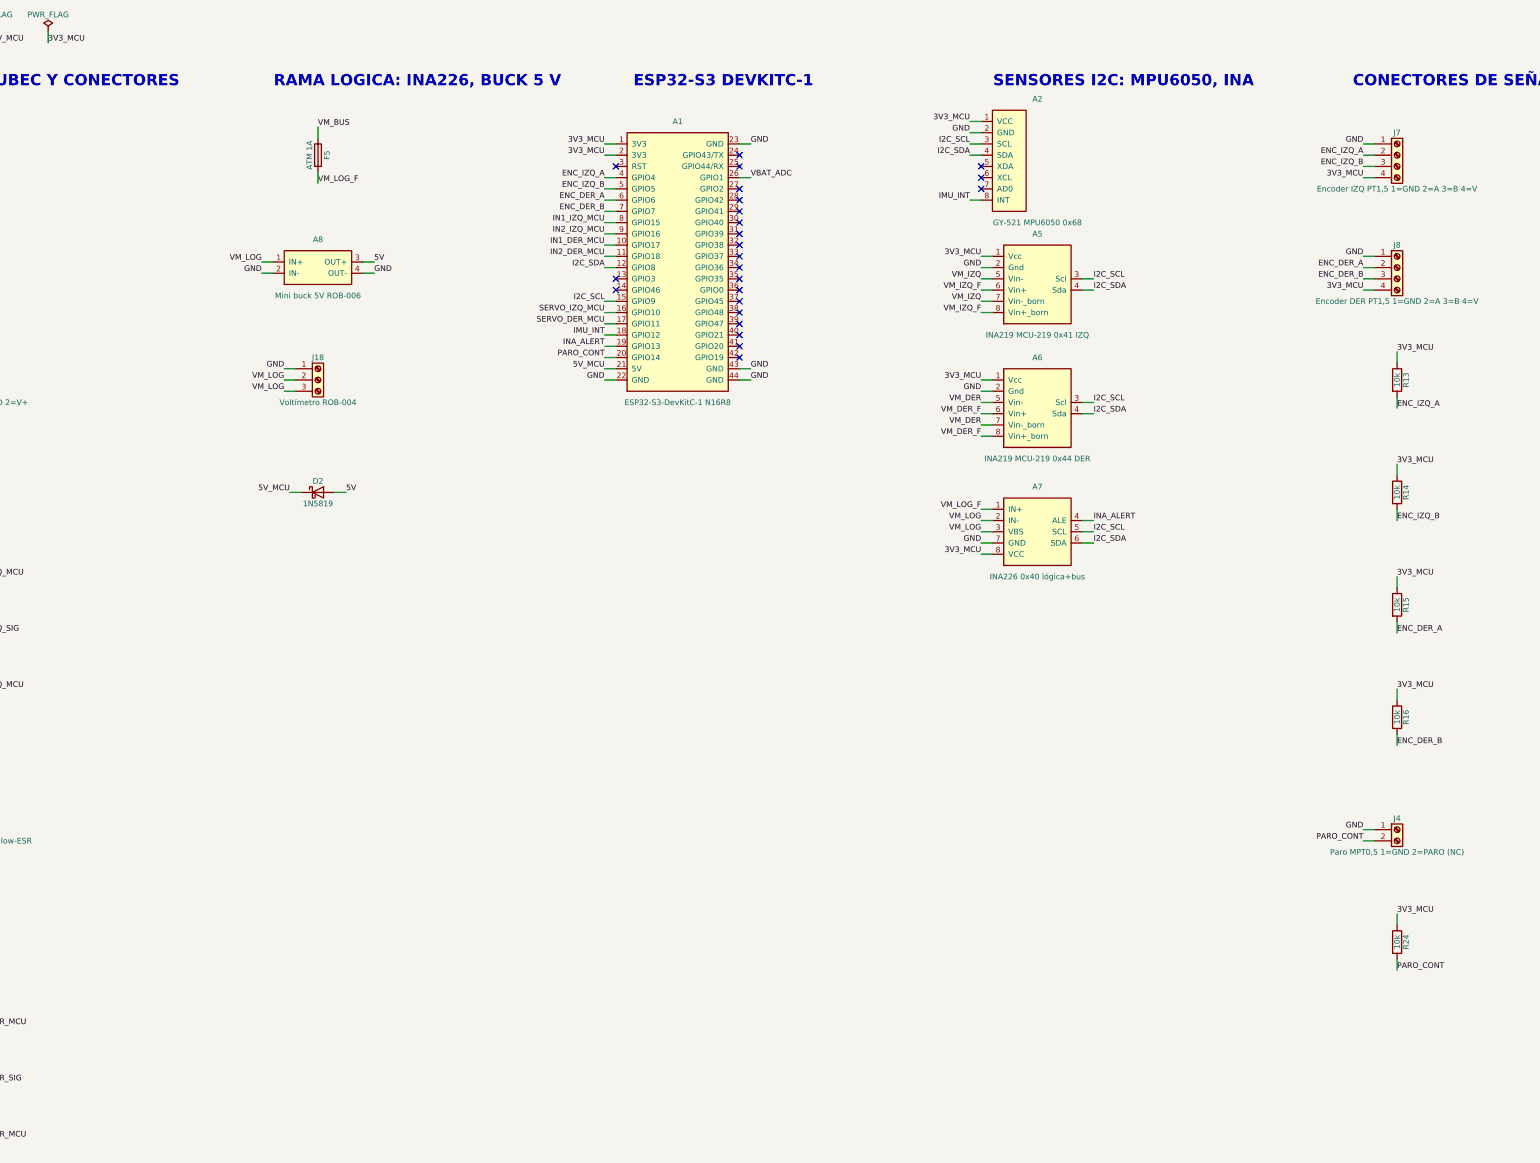
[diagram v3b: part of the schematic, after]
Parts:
- removed A1: Blue Pill STM32F103C8T6, segway_modulos:ROB-012_BluePill_STM32F103C8_40p, symbol segway_modulos:ROB-012_BluePill_STM32F103C8_40p
- removed A9: Mini buck 3,3V ROB-005 (3V3_PER), segway_modulos:ROB-005-006_MiniBuck_modulo_4p, symbol segway_modulos:ROB-005-006_MiniBuck_modulo_4p
- removed J23: UART1 1=GND 2=TX 3=RX, Connector_PinHeader_2.54mm:PinHeader_1x03_P2.54mm_Vertical, symbol Connector_Generic:Conn_01x03
- added A1: ESP32-S3-DevKitC-1 N16R8, segway_modulos:ROB-012_ESP32-S3-DevKitC-1_N16R8_44p, symbol segway_modulos:ROB-012_ESP32-S3-DevKitC-1_N16R8_44p
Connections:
- net 3V3_PER is gone; now on net 3V3_MCU: A2.1 (VCC), A5.1 (Vcc), A6.1 (Vcc), A7.8 (VCC), J7.4 (Pin_4), J8.4 (Pin_4), R13.1, R14.1, R15.1, R16.1
- net 3V3_MCU: now also A1.1 (3V3), A1.2 (3V3)
- net 5V_MCU: now also A1.21 (5V)
- net ENC_DER_A: now also A1.6 (GPIO6)
- net ENC_DER_B: now also A1.7 (GPIO7)
- net ENC_IZQ_A: now also A1.4 (GPIO4)
- net ENC_IZQ_B: now also A1.5 (GPIO5)
- net GND: now also A1.22 (GND), A1.23 (GND), A1.43 (GND), A1.44 (GND)
- net I2C_SCL: now also A1.15 (GPIO9)
- net I2C_SDA: now also A1.12 (GPIO8)
- net IMU_INT: now also A1.18 (GPIO12)
- net IN1_DER_MCU: now also A1.10 (GPIO17)
- net IN1_IZQ_MCU: now also A1.8 (GPIO15)
- net IN2_DER_MCU: now also A1.11 (GPIO18)
- net IN2_IZQ_MCU: now also A1.9 (GPIO16)
- net INA_ALERT: now also A1.19 (GPIO13)
- net PARO_CONT: now also A1.20 (GPIO14)
- net SERVO_DER_MCU: now also A1.17 (GPIO11)
- net SERVO_IZQ_MCU: now also A1.16 (GPIO10)
- net VBAT_ADC: now also A1.26 (GPIO1)
- no-connect marks 19 -> 24
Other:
- note added: "ESP32-S3 DEVKITC-1"
- note removed: "BLUE PILL STM32"
